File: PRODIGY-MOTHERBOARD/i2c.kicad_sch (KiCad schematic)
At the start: 7 parts, among them U13 PCA9306DC, U14 SN74LVC1T45DBV

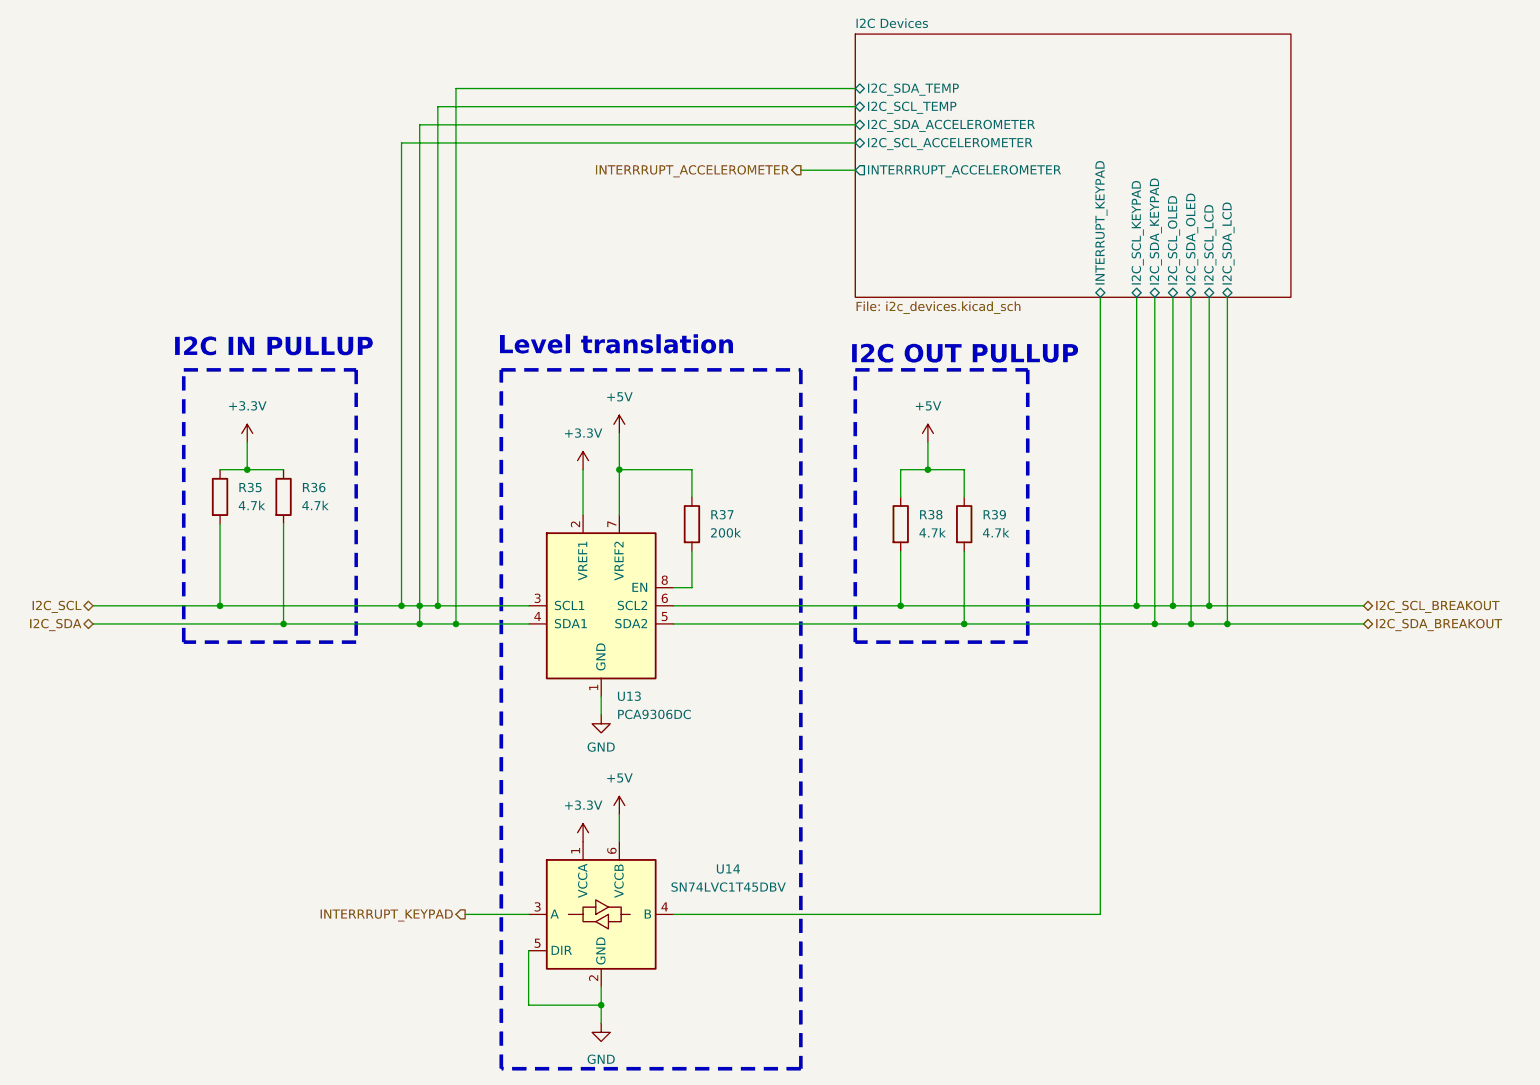
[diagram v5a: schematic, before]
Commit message: Submitted V0 for evaluation. Avaiting feedback.
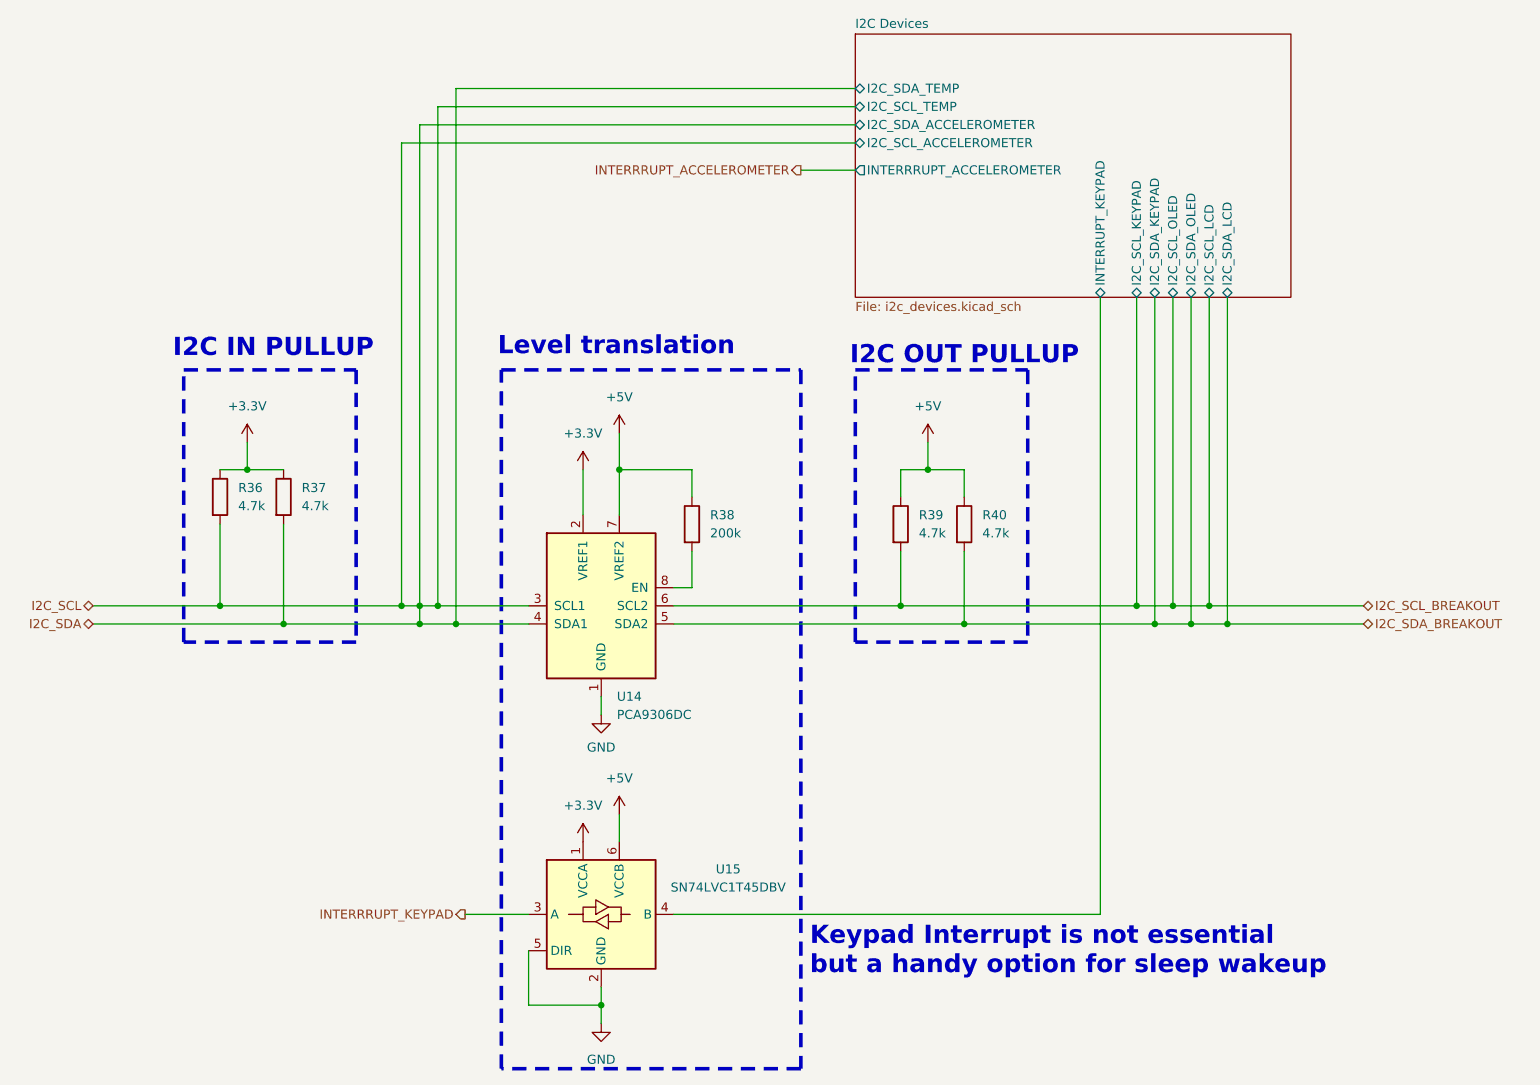
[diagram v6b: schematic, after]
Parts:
- renumbered R35 to R36, R36 to R37, R37 to R38, R38 to R39, R39 to R40, U13 to U14, U14 to U15
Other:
- note added: "Keypad Interrupt is not essential but a handy option for sleep wakeup"
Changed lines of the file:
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@@
+		)
+	)
+	(text "Keypad Interrupt is not essential\nbut a handy option for sleep wakeup"
+		(exclude_from_sim no)
+		(at 160.02 158.496 0)
+		(effects
+			(font
+				(size 2.54 2.54)
+				(thickness 0.508)
+				(bold yes)
+			)
+			(justify left bottom)
 		)
 	)
@@
 		(dnp no)
 		(fields_autoplaced yes)
-		(property "Reference" "U14"
+		(property "Reference" "U15"
 			(at 148.59 143.5414 0)
 			(effects
@@
 			(project "PRODIGY-MOTHERBOARD"
 				(path "/f1c25860-8989-4190-bd24-2491d23ca7d9/68745e9f-546d-4e12-ac2b-ba23aeab0093"
-					(reference "U14")
+					(reference "U15")
 					(unit 1)
 				)
@@
 		(dnp no)
 		(fields_autoplaced yes)
-		(property "Reference" "U13"
+		(property "Reference" "U14"
 			(at 133.0041 119.38 0)
 			(effects
@@
 			(project "PRODIGY-MOTHERBOARD"
 				(path "/f1c25860-8989-4190-bd24-2491d23ca7d9/68745e9f-546d-4e12-ac2b-ba23aeab0093"
-					(reference "U13")
+					(reference "U14")
 					(unit 1)
 				)
@@
 		(dnp no)
 		(fields_autoplaced yes)
-		(property "Reference" "R39"
+		(property "Reference" "R40"
 			(at 184.15 93.9799 0)
 			(effects
@@
 			(project "PRODIGY-MOTHERBOARD"
 				(path "/f1c25860-8989-4190-bd24-2491d23ca7d9/68745e9f-546d-4e12-ac2b-ba23aeab0093"
-					(reference "R39")
+					(reference "R40")
 					(unit 1)
 				)
@@
 		(dnp no)
 		(fields_autoplaced yes)
-		(property "Reference" "#PWR081"
+		(property "Reference" "#PWR0110"
 			(at 133.35 86.36 0)
 			(effects
@@
 			(project "PRODIGY-MOTHERBOARD"
 				(path "/f1c25860-8989-4190-bd24-2491d23ca7d9/68745e9f-546d-4e12-ac2b-ba23aeab0093"
-					(reference "#PWR081")
+					(reference "#PWR0110")
 					(unit 1)
 				)
@@
 		(dnp no)
 		(fields_autoplaced yes)
-		(property "Reference" "R36"
+		(property "Reference" "R37"
 			(at 88.9 90.1699 0)
 			(effects
@@
 			(project "PRODIGY-MOTHERBOARD"
 				(path "/f1c25860-8989-4190-bd24-2491d23ca7d9/68745e9f-546d-4e12-ac2b-ba23aeab0093"
-					(reference "R36")
+					(reference "R37")
 					(unit 1)
 				)
@@
 		(dnp no)
 		(fields_autoplaced yes)
-		(property "Reference" "#PWR084"
+		(property "Reference" "#PWR0113"
 			(at 128.27 91.44 0)
 			(effects
@@
 			(project "PRODIGY-MOTHERBOARD"
 				(path "/f1c25860-8989-4190-bd24-2491d23ca7d9/68745e9f-546d-4e12-ac2b-ba23aeab0093"
-					(reference "#PWR084")
+					(reference "#PWR0113")
 					(unit 1)
 				)
@@
 		(dnp no)
 		(fields_autoplaced yes)
-		(property "Reference" "#PWR083"
+		(property "Reference" "#PWR0112"
 			(at 176.53 87.63 0)
 			(effects
@@
 			(project "PRODIGY-MOTHERBOARD"
 				(path "/f1c25860-8989-4190-bd24-2491d23ca7d9/68745e9f-546d-4e12-ac2b-ba23aeab0093"
-					(reference "#PWR083")
+					(reference "#PWR0112")
 					(unit 1)
 				)
@@
 		(dnp no)
 		(fields_autoplaced yes)
-		(property "Reference" "#PWR082"
+		(property "Reference" "#PWR0111"
 			(at 81.28 87.63 0)
 			(effects
@@
 			(project "PRODIGY-MOTHERBOARD"
 				(path "/f1c25860-8989-4190-bd24-2491d23ca7d9/68745e9f-546d-4e12-ac2b-ba23aeab0093"
-					(reference "#PWR082")
+					(reference "#PWR0111")
 					(unit 1)
 				)
@@
 		(on_board yes)
 		(dnp no)
-		(property "Reference" "#PWR085"
+		(property "Reference" "#PWR0114"
 			(at 130.81 128.27 0)
 			(effects
@@
 			(project "PRODIGY-MOTHERBOARD"
 				(path "/f1c25860-8989-4190-bd24-2491d23ca7d9/68745e9f-546d-4e12-ac2b-ba23aeab0093"
-					(reference "#PWR085")
+					(reference "#PWR0114")
 					(unit 1)
 				)
@@
 		(dnp no)
 		(fields_autoplaced yes)
-		(property "Reference" "#PWR088"
+		(property "Reference" "#PWR0117"
 			(at 130.81 171.45 0)
 			(effects
@@
 			(project "PRODIGY-MOTHERBOARD"
 				(path "/f1c25860-8989-4190-bd24-2491d23ca7d9/68745e9f-546d-4e12-ac2b-ba23aeab0093"
-					(reference "#PWR088")
+					(reference "#PWR0117")
 					(unit 1)
 				)
@@
 		(dnp no)
 		(fields_autoplaced yes)
-		(property "Reference" "R38"
+		(property "Reference" "R39"
 			(at 175.26 93.9799 0)
 			(effects
@@
 			(project "PRODIGY-MOTHERBOARD"
 				(path "/f1c25860-8989-4190-bd24-2491d23ca7d9/68745e9f-546d-4e12-ac2b-ba23aeab0093"
-					(reference "R38")
+					(reference "R39")
 					(unit 1)
 				)
@@
 		(dnp no)
 		(fields_autoplaced yes)
-		(property "Reference" "#PWR086"
+		(property "Reference" "#PWR0115"
 			(at 133.35 139.7 0)
 			(effects
@@
 			(project "PRODIGY-MOTHERBOARD"
 				(path "/f1c25860-8989-4190-bd24-2491d23ca7d9/68745e9f-546d-4e12-ac2b-ba23aeab0093"
-					(reference "#PWR086")
+					(reference "#PWR0115")
 					(unit 1)
 				)
@@
 		(dnp no)
 		(fields_autoplaced yes)
-		(property "Reference" "#PWR087"
+		(property "Reference" "#PWR0116"
 			(at 128.27 143.51 0)
 			(effects
@@
 			(project "PRODIGY-MOTHERBOARD"
 				(path "/f1c25860-8989-4190-bd24-2491d23ca7d9/68745e9f-546d-4e12-ac2b-ba23aeab0093"
-					(reference "#PWR087")
+					(reference "#PWR0116")
 					(unit 1)
 				)
@@
 		(dnp no)
 		(fields_autoplaced yes)
-		(property "Reference" "R37"
+		(property "Reference" "R38"
 			(at 146.05 93.9799 0)
 			(effects
@@
 			(project "PRODIGY-MOTHERBOARD"
 				(path "/f1c25860-8989-4190-bd24-2491d23ca7d9/68745e9f-546d-4e12-ac2b-ba23aeab0093"
-					(reference "R37")
+					(reference "R38")
 					(unit 1)
 				)
@@
 		(dnp no)
 		(fields_autoplaced yes)
-		(property "Reference" "R35"
+		(property "Reference" "R36"
 			(at 80.01 90.1699 0)
 			(effects
@@
 			(project "PRODIGY-MOTHERBOARD"
 				(path "/f1c25860-8989-4190-bd24-2491d23ca7d9/68745e9f-546d-4e12-ac2b-ba23aeab0093"
-					(reference "R35")
+					(reference "R36")
 					(unit 1)
 				)
@@
 			(project "PRODIGY-MOTHERBOARD"
 				(path "/f1c25860-8989-4190-bd24-2491d23ca7d9/68745e9f-546d-4e12-ac2b-ba23aeab0093"
-					(page "19")
-				)
-			)
+					(page "9")
+				)
+			)

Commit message: Finished v0.1 schematic.
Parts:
- renumbered R36 to R27, R37 to R28, R38 to R29, R39 to R30, R40 to R31, U14 to U7, U15 to U8
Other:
- note removed: "Keypad Interrupt is not essential but a handy option for sleep wakeup"
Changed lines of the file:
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@@
-		)
-	)
-	(text "Keypad Interrupt is not essential\nbut a handy option for sleep wakeup"
-		(exclude_from_sim no)
-		(at 160.02 158.496 0)
-		(effects
-			(font
-				(size 2.54 2.54)
-				(thickness 0.508)
-				(bold yes)
-			)
-			(justify left bottom)
 		)
 	)
@@
 		(dnp no)
 		(fields_autoplaced yes)
-		(property "Reference" "U15"
+		(property "Reference" "U8"
 			(at 148.59 143.5414 0)
 			(effects
@@
 			(project "PRODIGY-MOTHERBOARD"
 				(path "/f1c25860-8989-4190-bd24-2491d23ca7d9/68745e9f-546d-4e12-ac2b-ba23aeab0093"
-					(reference "U15")
+					(reference "U8")
 					(unit 1)
 				)
@@
 		(dnp no)
 		(fields_autoplaced yes)
-		(property "Reference" "U14"
+		(property "Reference" "U7"
 			(at 133.0041 119.38 0)
 			(effects
@@
 			(project "PRODIGY-MOTHERBOARD"
 				(path "/f1c25860-8989-4190-bd24-2491d23ca7d9/68745e9f-546d-4e12-ac2b-ba23aeab0093"
-					(reference "U14")
+					(reference "U7")
 					(unit 1)
 				)
@@
 		(dnp no)
 		(fields_autoplaced yes)
-		(property "Reference" "R40"
+		(property "Reference" "R31"
 			(at 184.15 93.9799 0)
 			(effects
@@
 			(project "PRODIGY-MOTHERBOARD"
 				(path "/f1c25860-8989-4190-bd24-2491d23ca7d9/68745e9f-546d-4e12-ac2b-ba23aeab0093"
-					(reference "R40")
+					(reference "R31")
 					(unit 1)
 				)
@@
 		(dnp no)
 		(fields_autoplaced yes)
-		(property "Reference" "#PWR0110"
+		(property "Reference" "#PWR0105"
 			(at 133.35 86.36 0)
 			(effects
@@
 			(project "PRODIGY-MOTHERBOARD"
 				(path "/f1c25860-8989-4190-bd24-2491d23ca7d9/68745e9f-546d-4e12-ac2b-ba23aeab0093"
-					(reference "#PWR0110")
+					(reference "#PWR0105")
 					(unit 1)
 				)
@@
 		(dnp no)
 		(fields_autoplaced yes)
-		(property "Reference" "R37"
+		(property "Reference" "R28"
 			(at 88.9 90.1699 0)
 			(effects
@@
 			(project "PRODIGY-MOTHERBOARD"
 				(path "/f1c25860-8989-4190-bd24-2491d23ca7d9/68745e9f-546d-4e12-ac2b-ba23aeab0093"
-					(reference "R37")
+					(reference "R28")
 					(unit 1)
 				)
@@
 		(dnp no)
 		(fields_autoplaced yes)
-		(property "Reference" "#PWR0113"
+		(property "Reference" "#PWR0101"
 			(at 128.27 91.44 0)
 			(effects
@@
 			(project "PRODIGY-MOTHERBOARD"
 				(path "/f1c25860-8989-4190-bd24-2491d23ca7d9/68745e9f-546d-4e12-ac2b-ba23aeab0093"
-					(reference "#PWR0113")
+					(reference "#PWR0101")
 					(unit 1)
 				)
@@
 		(dnp no)
 		(fields_autoplaced yes)
-		(property "Reference" "#PWR0112"
+		(property "Reference" "#PWR0107"
 			(at 176.53 87.63 0)
 			(effects
@@
 			(project "PRODIGY-MOTHERBOARD"
 				(path "/f1c25860-8989-4190-bd24-2491d23ca7d9/68745e9f-546d-4e12-ac2b-ba23aeab0093"
-					(reference "#PWR0112")
+					(reference "#PWR0107")
 					(unit 1)
 				)
@@
 		(dnp no)
 		(fields_autoplaced yes)
-		(property "Reference" "#PWR0111"
+		(property "Reference" "#PWR0100"
 			(at 81.28 87.63 0)
 			(effects
@@
 			(project "PRODIGY-MOTHERBOARD"
 				(path "/f1c25860-8989-4190-bd24-2491d23ca7d9/68745e9f-546d-4e12-ac2b-ba23aeab0093"
-					(reference "#PWR0111")
+					(reference "#PWR0100")
 					(unit 1)
 				)
@@
 		(on_board yes)
 		(dnp no)
-		(property "Reference" "#PWR0114"
+		(property "Reference" "#PWR0103"
 			(at 130.81 128.27 0)
 			(effects
@@
 			(project "PRODIGY-MOTHERBOARD"
 				(path "/f1c25860-8989-4190-bd24-2491d23ca7d9/68745e9f-546d-4e12-ac2b-ba23aeab0093"
-					(reference "#PWR0114")
+					(reference "#PWR0103")
 					(unit 1)
 				)
@@
 		(dnp no)
 		(fields_autoplaced yes)
-		(property "Reference" "#PWR0117"
+		(property "Reference" "#PWR0104"
 			(at 130.81 171.45 0)
 			(effects
@@
 			(project "PRODIGY-MOTHERBOARD"
 				(path "/f1c25860-8989-4190-bd24-2491d23ca7d9/68745e9f-546d-4e12-ac2b-ba23aeab0093"
-					(reference "#PWR0117")
+					(reference "#PWR0104")
 					(unit 1)
 				)
@@
 		(dnp no)
 		(fields_autoplaced yes)
-		(property "Reference" "R39"
+		(property "Reference" "R30"
 			(at 175.26 93.9799 0)
 			(effects
@@
 			(project "PRODIGY-MOTHERBOARD"
 				(path "/f1c25860-8989-4190-bd24-2491d23ca7d9/68745e9f-546d-4e12-ac2b-ba23aeab0093"
-					(reference "R39")
+					(reference "R30")
 					(unit 1)
 				)
@@
 		(dnp no)
 		(fields_autoplaced yes)
-		(property "Reference" "#PWR0115"
+		(property "Reference" "#PWR0106"
 			(at 133.35 139.7 0)
 			(effects
@@
 			(project "PRODIGY-MOTHERBOARD"
 				(path "/f1c25860-8989-4190-bd24-2491d23ca7d9/68745e9f-546d-4e12-ac2b-ba23aeab0093"
-					(reference "#PWR0115")
+					(reference "#PWR0106")
 					(unit 1)
 				)
@@
 		(dnp no)
 		(fields_autoplaced yes)
-		(property "Reference" "#PWR0116"
+		(property "Reference" "#PWR0102"
 			(at 128.27 143.51 0)
 			(effects
@@
 			(project "PRODIGY-MOTHERBOARD"
 				(path "/f1c25860-8989-4190-bd24-2491d23ca7d9/68745e9f-546d-4e12-ac2b-ba23aeab0093"
-					(reference "#PWR0116")
+					(reference "#PWR0102")
 					(unit 1)
 				)
@@
 		(dnp no)
 		(fields_autoplaced yes)
-		(property "Reference" "R38"
+		(property "Reference" "R29"
 			(at 146.05 93.9799 0)
 			(effects
@@
 			(project "PRODIGY-MOTHERBOARD"
 				(path "/f1c25860-8989-4190-bd24-2491d23ca7d9/68745e9f-546d-4e12-ac2b-ba23aeab0093"
-					(reference "R38")
+					(reference "R29")
 					(unit 1)
 				)
@@
 		(dnp no)
 		(fields_autoplaced yes)
-		(property "Reference" "R36"
+		(property "Reference" "R27"
 			(at 80.01 90.1699 0)
 			(effects
@@
 			(project "PRODIGY-MOTHERBOARD"
 				(path "/f1c25860-8989-4190-bd24-2491d23ca7d9/68745e9f-546d-4e12-ac2b-ba23aeab0093"
-					(reference "R36")
-					(unit 1)
-				)
+					(reference "R27")
+					(unit 1)
+				)
